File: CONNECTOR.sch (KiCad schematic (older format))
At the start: 0 parts

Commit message: Added pdata lines and ran bus connections
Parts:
- added J2: QTH-030-02-L-DA, QTH_030_02:QTH-030-02-L-D-A, symbol QTH-030-02-L-DA
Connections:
- new net PDATA0: J2.9 (A5)
- new net PDATA1: J2.1 (A1)
- new net PDATA10: J2.8 (B4)
- new net PDATA11: J2.21 (A11)
- new net PDATA12: J2.10 (B5)
- new net PDATA13: J2.25 (A13)
- new net PDATA14: J2.12 (B6)
- new net PDATA15: J2.29 (A15)
- new net PDATA16: J2.14 (B7)
- new net PDATA17: J2.33 (A17)
- new net PDATA18: J2.16 (B8)
- new net PDATA19: J2.37 (A19)
- new net PDATA2: J2.11 (A6)
- new net PDATA20: J2.18 (B9)
- new net PDATA21: J2.41 (A21)
- new net PDATA22: J2.20 (B10)
- new net PDATA23: J2.45 (A23)
- new net PDATA3: J2.3 (A2)
- new net PDATA4: J2.13 (A7)
- new net PDATA5: J2.5 (A3)
- new net PDATA6: J2.15 (A8)
- new net PDATA7: J2.7 (A4)
- new net PDATA8: J2.4 (B2)
- new net PDATA9: J2.6 (B3)
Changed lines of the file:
@@
 LIBS:xtal
 LIBS:tpd4S010
+LIBS:QTH-030-02-L-DA
+LIBS:rpack
 LIBS:HDMI2RGB-cache
 EELAYER 25 0
 EELAYER END
-$Descr A4 11693 8268
+$Descr B 17000 11000
 encoding utf-8
 Sheet 3 5
-Title ""
-Date ""
-Rev ""
+Title "DLP CONNECTION - TO DLP3010 EVM"
+Date "Sun 27 Mar 2016"
+Rev "1.1"
 Comp ""
 Comment1 ""
@@
 Comment4 ""
 $EndDescr
+$Comp
+L QTH-030-02-L-DA J2
+U 1 1 56F986F9
+P 7800 4950
+F 0 "J2" H 7400 6750 50  0000 C CNN
+F 1 "QTH-030-02-L-DA" H 8400 3400 50  0000 C CNN
+F 2 "QTH_030_02:QTH-030-02-L-D-A" H 7800 4950 50  0001 C CNN
+F 3 "DOCUMENTATION" H 7800 4950 50  0001 C CNN
+F 4 "9.88" H 8000 5050 60  0001 C CNN "Cost"
+F 5 "Digikey" H 8200 5250 60  0001 C CNN "Supplier"
+F 6 "http://www.digikey.com/product-detail/en/samtec-inc/QTH-030-02-L-D-A/SAM8186-ND/1106530" H 8100 5150 60  0001 C CNN "Link"
+F 7 "QTH-030-L-D-A" H 7900 4950 60  0001 C CNN "Part #"
+	1    7800 4950
+	-1   0    0    -1
+$EndComp
+Text GLabel 4900 2700 0    60   Input ~ 0
+PDATA[0..23]
+Wire Bus Line
+	4900 2700 9300 2700
+Wire Bus Line
+	6300 2700 6300 4250
+Wire Bus Line
+	9300 2700 9300 5750
+Entry Wire Line
+	6300 3800 6400 3900
+Entry Wire Line
+	6300 3500 6400 3600
+Entry Wire Line
+	6300 3600 6400 3700
+Entry Wire Line
+	6300 3700 6400 3800
+Wire Wire Line
+	7050 3600 6400 3600
+Wire Wire Line
+	7050 3700 6400 3700
+Wire Wire Line
+	7050 3800 6400 3800
+Wire Wire Line
+	6400 3900 7050 3900
+Entry Wire Line
+	6300 3900 6400 4000
+Entry Wire Line
+	6300 4000 6400 4100
+Entry Wire Line
+	6300 4100 6400 4200
+Entry Wire Line
+	6300 4200 6400 4300
+Wire Wire Line
+	7050 4000 6400 4000
+Wire Wire Line
+	7050 4100 6400 4100
+Wire Wire Line
+	7050 4200 6400 4200
+Wire Wire Line
+	7050 4300 6400 4300
+Entry Wire Line
+	9300 3300 9200 3400
+Entry Wire Line
+	9300 3500 9200 3600
+Entry Wire Line
+	9300 3700 9200 3800
+Entry Wire Line
+	9300 3900 9200 4000
+Wire Wire Line
+	8550 3400 9200 3400
+Wire Wire Line
+	8550 3600 9200 3600
+Wire Wire Line
+	8550 3800 9200 3800
+Wire Wire Line
+	8550 4000 9200 4000
+Entry Wire Line
+	9300 4300 9200 4400
+Entry Wire Line
+	9300 4500 9200 4600
+Entry Wire Line
+	9300 4700 9200 4800
+Entry Wire Line
+	9300 4900 9200 5000
+Wire Wire Line
+	8550 4400 9200 4400
+Wire Wire Line
+	8550 4600 9200 4600
+Wire Wire Line
+	8550 4800 9200 4800
+Wire Wire Line
+	8550 5000 9200 5000
+Entry Wire Line
+	6300 3400 6400 3500
+Wire Wire Line
+	7050 3500 6400 3500
+Text Label 8750 3800 0    60   ~ 0
+PDATA0
+Text Label 8750 3400 0    60   ~ 0
+PDATA1
+Text Label 8750 3900 0    60   ~ 0
+PDATA2
+Text Label 8750 3500 0    60   ~ 0
+PDATA3
+Text Label 8750 4000 0    60   ~ 0
+PDATA4
+Text Label 8750 3600 0    60   ~ 0
+PDATA5
+Text Label 8750 4100 0    60   ~ 0
+PDATA6
+Text Label 8750 3700 0    60   ~ 0
+PDATA7
+Text Label 6550 3500 0    60   ~ 0
+PDATA8
+Text Label 6550 3600 0    60   ~ 0
+PDATA9
+Text Label 6550 3700 0    60   ~ 0
+PDATA10
+Text Label 8750 4400 0    60   ~ 0
+PDATA11
+Text Label 6550 3800 0    60   ~ 0
+PDATA12
+Text Label 8750 4600 0    60   ~ 0
+PDATA13
+Text Label 6550 3900 0    60   ~ 0
+PDATA14
+Text Label 8750 4800 0    60   ~ 0
+PDATA15
+Text Label 6550 4000 0    60   ~ 0
+PDATA16
+Text Label 8750 5000 0    60   ~ 0
+PDATA17
+Text Label 6550 4100 0    60   ~ 0
+PDATA18
+Text Label 8750 5200 0    60   ~ 0
+PDATA19
+Text Label 6550 4200 0    60   ~ 0
+PDATA20
+Text Label 8750 5400 0    60   ~ 0
+PDATA21
+Text Label 6550 4300 0    60   ~ 0
+PDATA22
+Text Label 8750 5600 0    60   ~ 0
+PDATA23
+Entry Wire Line
+	9300 4000 9200 4100
+Entry Wire Line
+	9300 3400 9200 3500
+Entry Wire Line
+	9300 3800 9200 3900
+Wire Wire Line
+	8550 3500 9200 3500
+Wire Wire Line
+	8550 3900 9200 3900
+Wire Wire Line
+	9200 4100 8550 4100
+Entry Wire Line
+	9200 5200 9300 5100
+Wire Wire Line
+	8550 5200 9200 5200
+Wire Wire Line
+	8550 5400 9200 5400
+Wire Wire Line
+	8550 5600 9200 5600
+Entry Wire Line
+	9200 5400 9300 5300
+Entry Wire Line
+	9200 5600 9300 5500
+Wire Wire Line
+	8550 3700 9200 3700
+Entry Wire Line
+	9200 3700 9300 3600
 $EndSCHEMATC

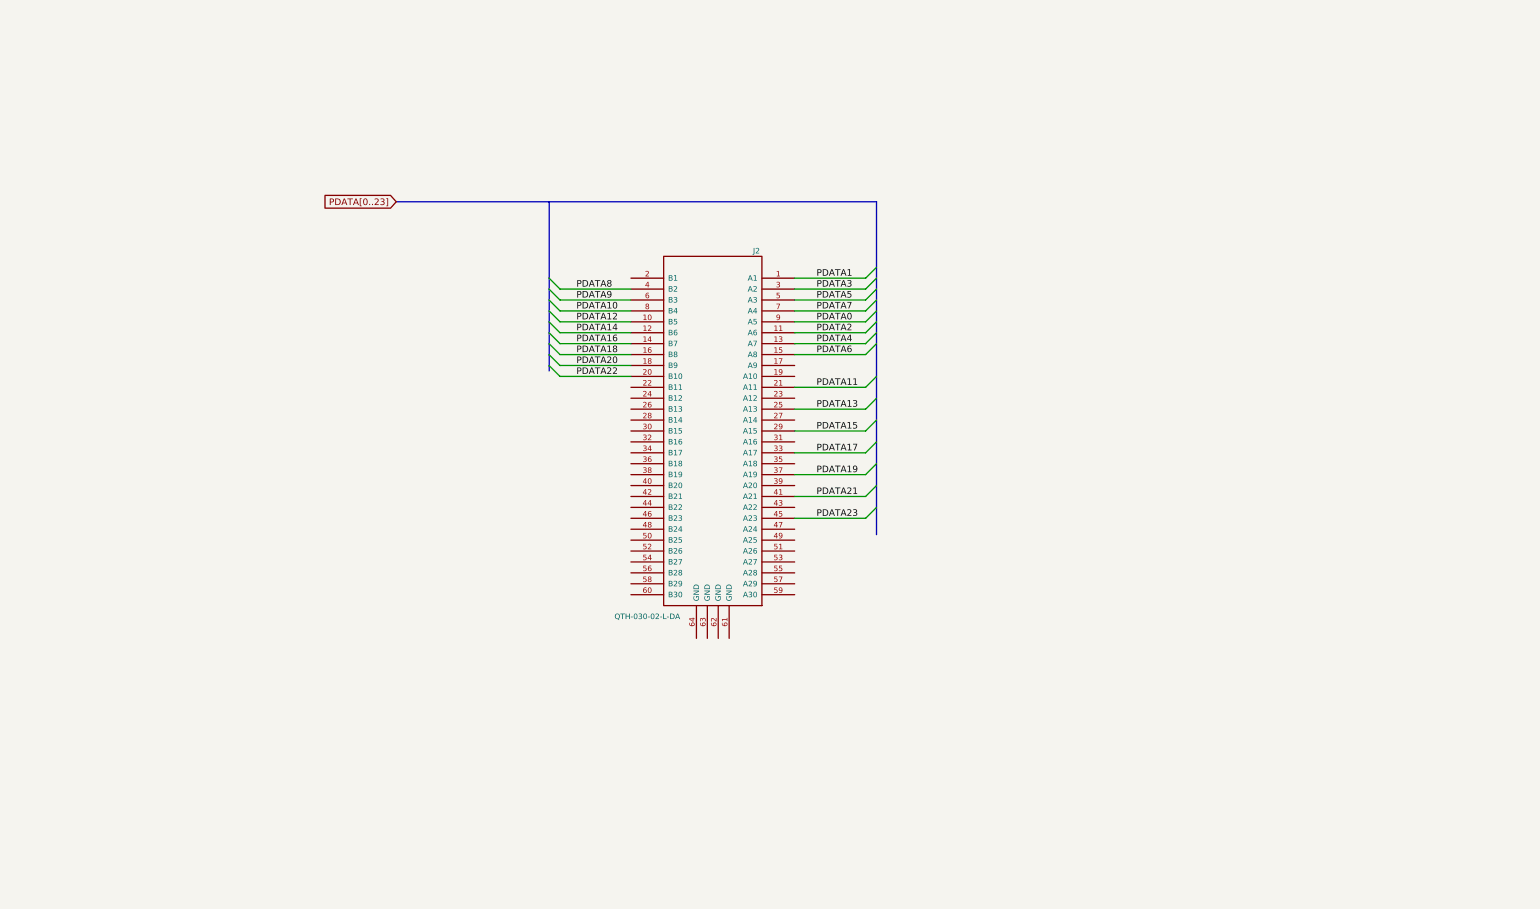
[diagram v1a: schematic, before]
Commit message: Started PCB Layout, added mounting holes, connectors, in correct locations
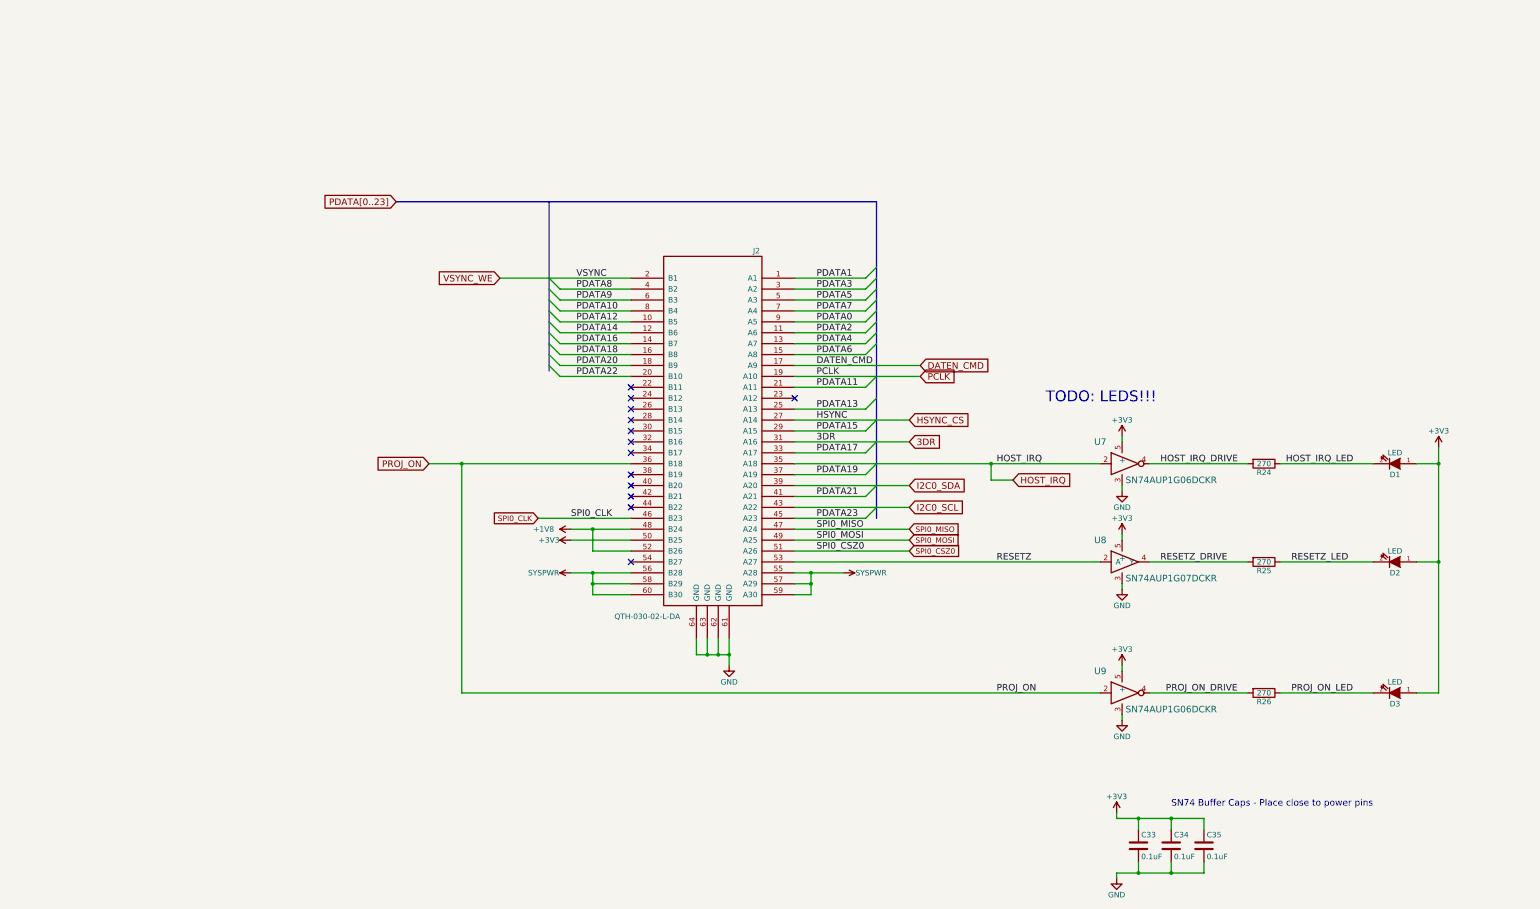
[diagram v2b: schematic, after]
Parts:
- added C33, C34, C35: 0.1uF, Capacitors_SMD:C_0402, symbol C
- added D1, D2, D3: LED, Capacitors_SMD:C_0603, symbol LED
- added R24, R25, R26: 270, Resistors_SMD:R_0402, symbol R
- added U7, U9: SN74AUP1G06DCKR, symbol SN74AUP1G06DCKR
- added U8: SN74AUP1G07DCKR, symbol SN74AUP1G07DCKR
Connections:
- net DATEN_CMD: now reaches J2.17 (A9)
- net PCLK: now reaches J2.19 (A10)
- net VSYNC_WE: now reaches J2.2 (B1)
- net HSYNC_CS: now reaches J2.27 (A14)
- net 3DR: now reaches J2.31 (A16)
- net HOST_IRQ: now reaches J2.35 (A18)
- net HOST_IRQ: now also U7.2
- net PROJ_ON: now reaches J2.36 (B18)
- net PROJ_ON: now also U9.2
- net I2C0_SDA: now reaches J2.39 (A20)
- net I2C0_SCL: now reaches J2.43 (A22)
- net SPI0_CLK: now reaches J2.46 (B23)
- net SPI0_MISO: now reaches J2.47 (A24)
- net +1V8: now reaches J2.48 (B24)
- net +1V8: now also J2.52 (B26)
- net SPI0_MOSI: now reaches J2.49 (A25)
- net +3V3: now reaches J2.50 (B25)
- net +3V3: now also C33.1, C34.1, C35.1, D1.1 (A), D2.1 (A), D3.1 (A), U7.5 (+), U8.5 (+), U9.5 (+)
- net SPI0_CSZ0: now reaches J2.51 (A26)
- net RESETZ: now reaches J2.53 (A27)
- net RESETZ: now also U8.2 (A)
- net SYSPWR: now reaches J2.55 (A28)
- net SYSPWR: now also J2.56 (B28), J2.57 (A29), J2.58 (B29), J2.59 (A30), J2.60 (B30)
- net GND: now reaches J2.61 (GND)
- net GND: now also J2.62 (GND), J2.63 (GND), J2.64 (GND), C33.2, C34.2, C35.2, U7.3, U8.3, U9.3
- new net HOST_IRQ_DRIVE: R24.2, U7.4
- new net HOST_IRQ_LED: D1.2 (K), R24.1
- new net PROJ_ON_DRIVE: R26.2, U9.4
- new net PROJ_ON_LED: D3.2 (K), R26.1
- new net RESETZ_DRIVE: R25.2, U8.4 (Y)
- new net RESETZ_LED: D2.2 (K), R25.1
- no-connect marks 0 -> 13
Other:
- note added: "SN74 Buffer Caps - Place close to power pins"
- note added: "TODO: LEDS!!!\n"

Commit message: Basic layout of all components on PCB
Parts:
- U7, U8, U9: footprint (none) -> TO_SOT_Packages_SMD:SC-70-5
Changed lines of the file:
@@
 F 0 "U7" H 11350 5300 60  0000 C CNN
 F 1 "SN74AUP1G06DCKR" H 12000 4950 60  0000 C CNN
-F 2 "" H 11450 5100 60  0001 C CNN
+F 2 "TO_SOT_Packages_SMD:SC-70-5" H 11450 5100 60  0001 C CNN
 F 3 "" H 11450 5100 60  0000 C CNN
 F 4 "SN74AUP1G06DCKR" H 11450 5400 60  0001 C CNN "Part #"
@@
 F 0 "U9" H 11350 7400 60  0000 C CNN
 F 1 "SN74AUP1G06DCKR" H 12000 7050 60  0000 C CNN
-F 2 "" H 11450 7200 60  0001 C CNN
+F 2 "TO_SOT_Packages_SMD:SC-70-5" H 11450 7200 60  0001 C CNN
 F 3 "" H 11450 7200 60  0000 C CNN
 F 4 "SN74AUP1G06DCKR" H 11450 7500 60  0001 C CNN "Part #"
@@
 F 0 "U8" H 11350 6200 60  0000 C CNN
 F 1 "SN74AUP1G07DCKR" H 12000 5850 60  0000 C CNN
-F 2 "" H 11450 6000 60  0001 C CNN
+F 2 "TO_SOT_Packages_SMD:SC-70-5" H 11450 6000 60  0001 C CNN
 F 3 "" H 11450 6000 60  0000 C CNN
 F 4 "SN74AUP1G07DCKR" H 11450 6300 60  0001 C CNN "Part #"

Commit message: First Final -- Waiting for Checker
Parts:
- added P2: CONN_01X06, Pin_Headers:Pin_Header_Straight_1x06, symbol CONN_01X06
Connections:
- net +3V3: now also P2.5 (P5)
- net GND: now also P2.6 (P6)
- net SPI0_CLK: now also P2.4 (P4)
- net SPI0_CSZ0: now also P2.1 (P1)
- net SPI0_MISO: now also P2.3 (P3)
- net SPI0_MOSI: now also P2.2 (P2)
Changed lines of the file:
@@
 $EndComp
 $Comp
-L SYSPWR #PWR20
+L SYSPWR #PWR22
 U 1 1 56F83223
 P 6500 6100
-F 0 "#PWR20" H 6550 6050 100 0001 C CNN
+F 0 "#PWR22" H 6550 6050 100 0001 C CNN
 F 1 "SYSPWR" V 6500 6350 50  0000 C CNN
 F 2 "" H 6500 6100 100 0000 C CNN
@@
 Connection ~ 11700 8850
 $Comp
-L SYSPWR #PWR22
+L SYSPWR #PWR24
 U 1 1 56F9621E
 P 9000 6100
-F 0 "#PWR22" H 9050 6050 100 0001 C CNN
+F 0 "#PWR24" H 9050 6050 100 0001 C CNN
 F 1 "SYSPWR" V 9000 6350 50  0000 C CNN
 F 2 "" H 9000 6100 100 0000 C CNN
@@
 	0    1    1    0
 $EndComp
+$Comp
+L CONN_01X06 P2
+U 1 1 56FD0D03
+P 1500 3700
+F 0 "P2" H 1500 4050 50  0000 C CNN
+F 1 "CONN_01X06" V 1600 3700 50  0000 C CNN
+F 2 "Pin_Headers:Pin_Header_Straight_1x06" H 1500 3700 60  0001 C CNN
+F 3 "" H 1500 3700 60  0000 C CNN
+	1    1500 3700
+	-1   0    0    -1
+$EndComp
+Text GLabel 2750 3650 2    50   Input ~ 0
+SPI0_MISO
+Text GLabel 2750 3550 2    50   Input ~ 0
+SPI0_MOSI
+Text GLabel 2750 3450 2    50   Input ~ 0
+SPI0_CSZ0
+Wire Wire Line
+	2750 3450 1700 3450
+Wire Wire Line
+	2750 3550 1700 3550
+Text Label 1900 3650 0    60   ~ 0
+SPI0_MISO
+Text Label 1900 3550 0    60   ~ 0
+SPI0_MOSI
+Text Label 1900 3450 0    60   ~ 0
+SPI0_CSZ0
+Wire Wire Line
+	2750 3650 1700 3650
+Text GLabel 2750 3750 2    50   Input ~ 0
+SPI0_CLK
+Wire Wire Line
+	2750 3750 1700 3750
+Text Label 2300 3750 2    60   ~ 0
+SPI0_CLK
+$Comp
+L +3V3 #PWR030
+U 1 1 56FD15FD
+P 3050 3850
+F 0 "#PWR030" H 3050 3700 50  0001 C CNN
+F 1 "+3V3" V 3050 4050 50  0000 C CNN
+F 2 "" H 3050 3850 60  0000 C CNN
+F 3 "" H 3050 3850 60  0000 C CNN
+	1    3050 3850
+	0    1    1    0
+$EndComp
+Wire Wire Line
+	1700 3850 3050 3850
+$Comp
+L GND #PWR031
+U 1 1 56FD175C
+P 1800 4000
+F 0 "#PWR031" H 1800 3750 50  0001 C CNN
+F 1 "GND" H 1800 3850 50  0000 C CNN
+F 2 "" H 1800 4000 60  0000 C CNN
+F 3 "" H 1800 4000 60  0000 C CNN
+	1    1800 4000
+	1    0    0    -1
+$EndComp
+Wire Wire Line
+	1700 3950 1800 3950
+Wire Wire Line
+	1800 3950 1800 4000
 $EndSCHEMATC

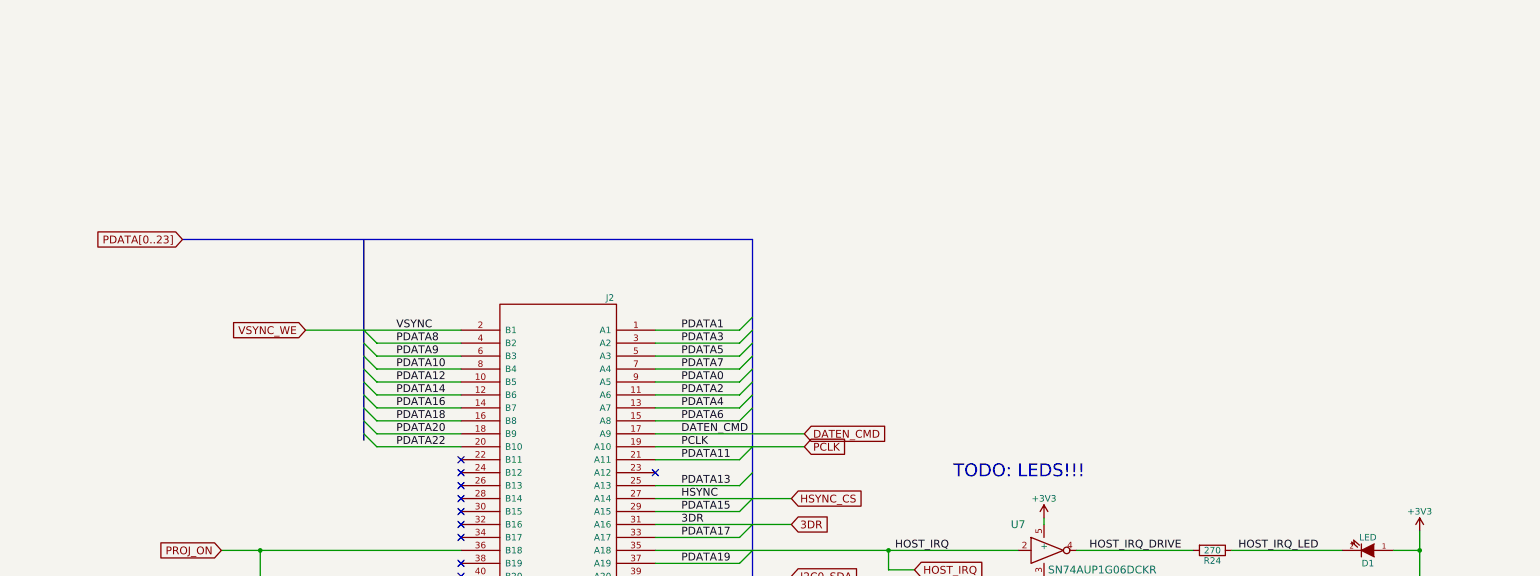
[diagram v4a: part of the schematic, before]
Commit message: Schematic Titles
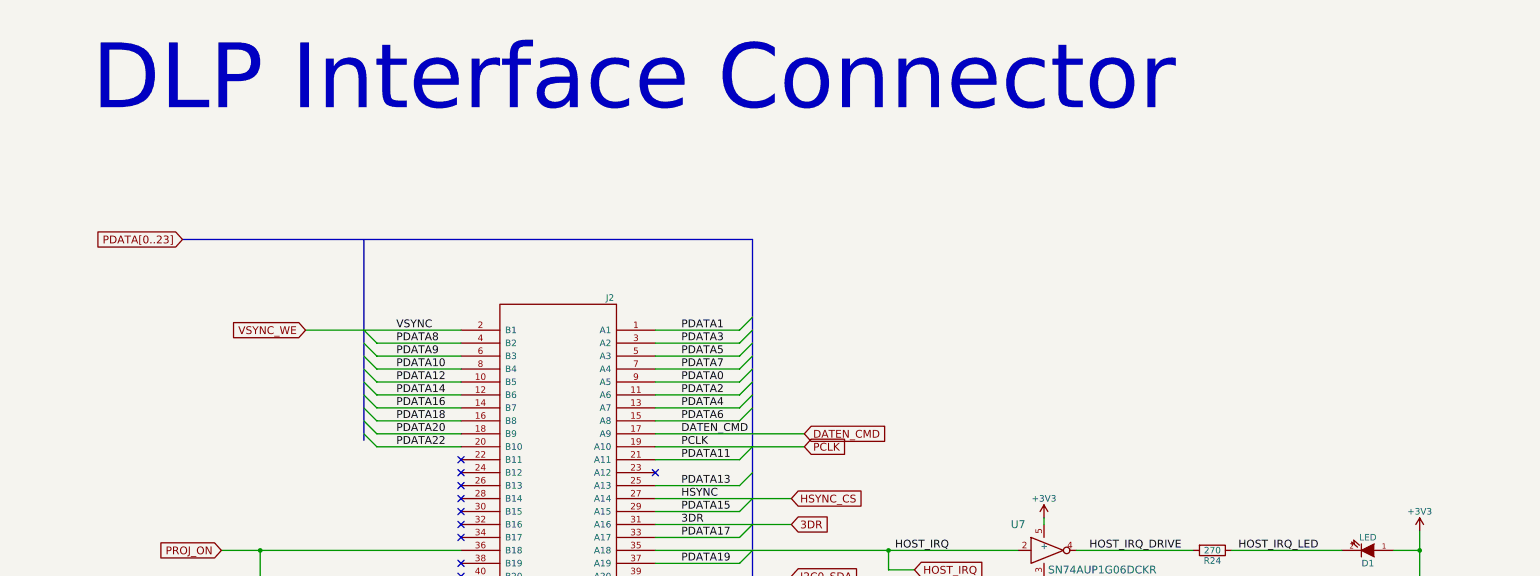
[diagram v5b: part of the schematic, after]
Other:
- note added: "DLP Interface Connector"
- note removed: "TODO: LEDS!!!\n"
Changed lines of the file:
@@
 Text Label 10400 5100 0    60   ~ 0
 HOST_IRQ
-Text Notes 10850 4550 0    100  ~ 0
-TODO: LEDS!!!\n
 Text GLabel 5200 5100 0    60   Input ~ 0
 PROJ_ON
@@
 Wire Wire Line
 	1800 3950 1800 4000
+Text Notes 4200 1750 0    500  ~ 0
+DLP Interface Connector
 $EndSCHEMATC
